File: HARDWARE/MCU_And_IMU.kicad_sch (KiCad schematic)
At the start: 16 parts, among them U2 STM32G431KBTx, Y1 Crystal_GND24

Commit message: Update footprints and add all PNs
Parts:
- BOOT_SW1: footprint (none) -> Button_Switch_THT_Custom:SW_SLW-883935-2A-D
- C11, C12, C13, C14, C15, C16: Part Number (none) -> 311-1341-2-ND
- CL1, CL2: Part Number (none) -> 311-3908-2-ND
- NRST1: footprint (none) -> Button_Switch_SMD_Custom:SW_Tactile_SPST_PTS636SK25FSMTRLFS; Part Number 108-PTS636SM43SMTRLFSTR-ND -> CKN12330-2-ND
- R4: Part Number (none) -> 311-10.0KHRTR-ND
- R5: Part Number (none) -> 311-68.0HRTR-ND
- STATUS1: footprint (none) -> LED_SMD_Custom:LED_APHBM2012QBDSURKC
- Y1: footprint (none) -> Crystal_Custom:XTAL_ECS-80-10-30B-CKM-TR
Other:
- note added: "NP0 (C0G) caps are used for the oscillator to keep frequency stable with temperature changes"
- moved on the sheet: BOOT_SW1, C11, C12, C13, C14, C15, C16, CL1, CL2, MT1, NRST1, R4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

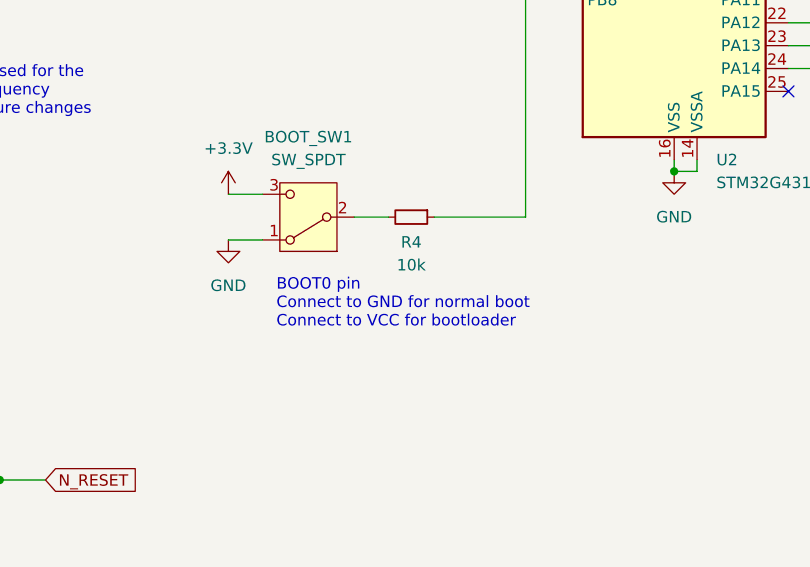
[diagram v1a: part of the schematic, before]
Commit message: Swap PWM channels and initial PCB layout
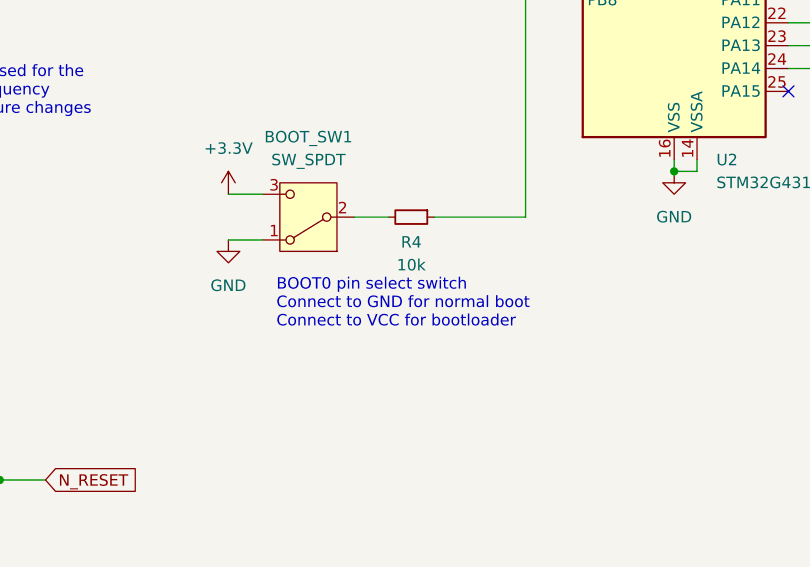
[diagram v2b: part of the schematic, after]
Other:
- note added: "BOOT0 pin select switch Connect to GND for normal boot Connect to VCC for bootloader"
- note removed: "BOOT0 pin Connect to GND for normal boot Connect to VCC for bootloader"
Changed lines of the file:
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@@
 		)
 	)
-	(text "BOOT0 pin\nConnect to GND for normal boot\nConnect to VCC for bootloader"
+	(text "BOOT0 pin select switch\nConnect to GND for normal boot\nConnect to VCC for bootloader"
 		(exclude_from_sim no)
 		(at 96.774 126.492 0)

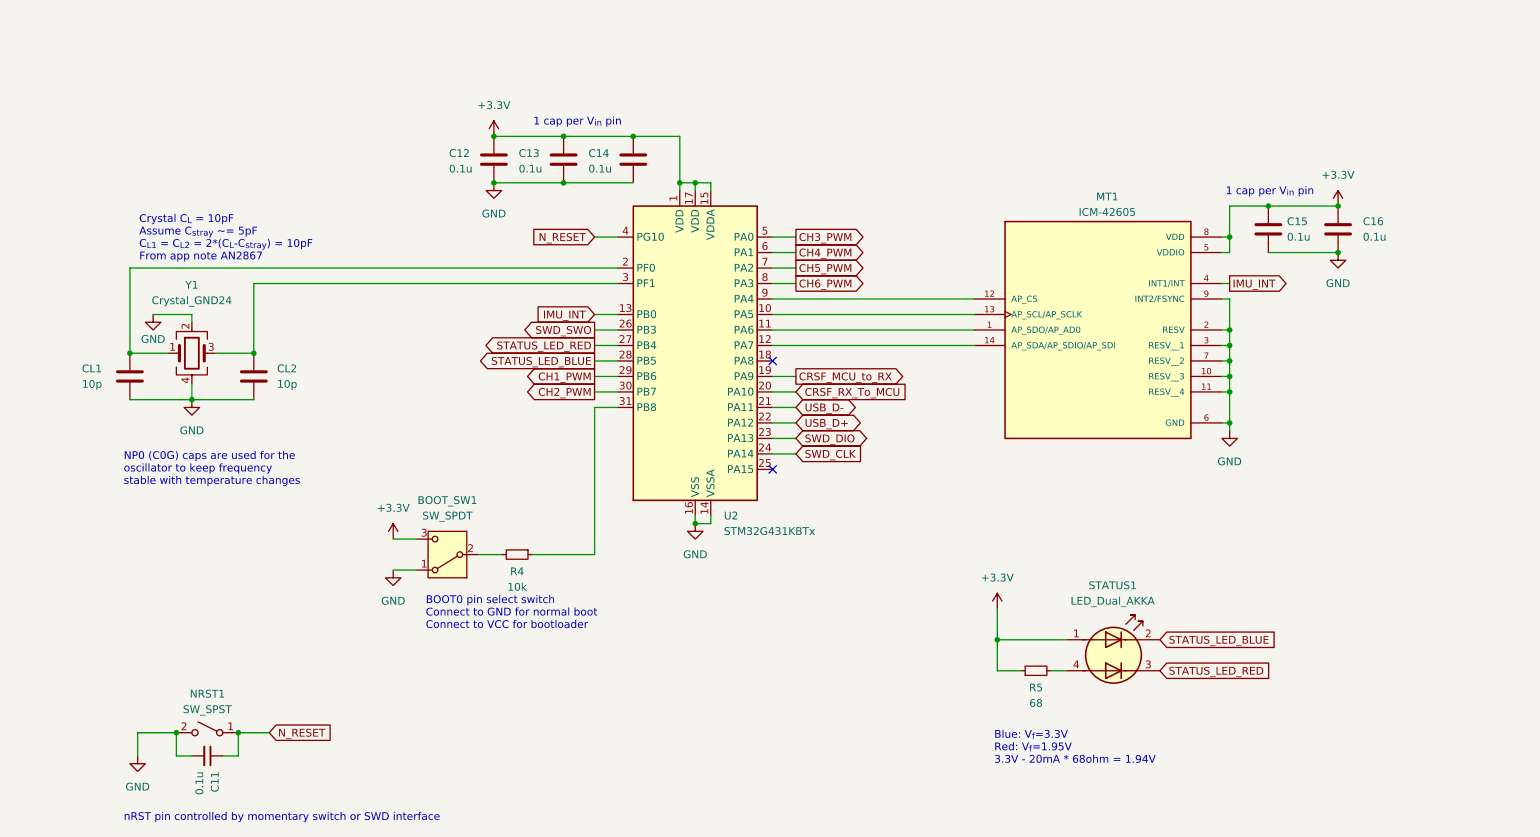
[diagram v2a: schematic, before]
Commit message: Update components and layout
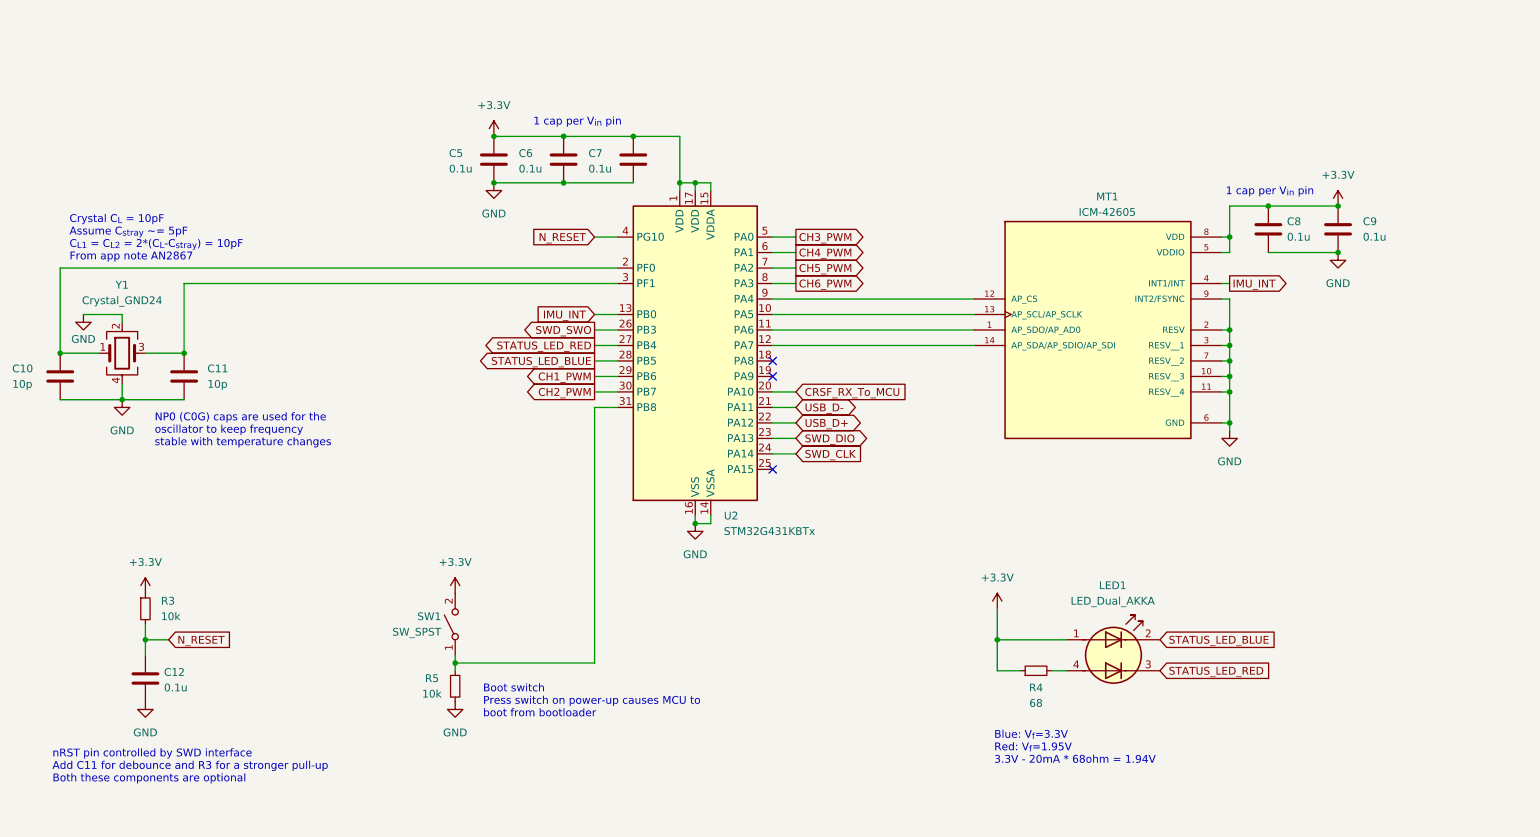
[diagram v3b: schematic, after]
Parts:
- removed BOOT_SW1: SW_SPDT, Button_Switch_THT_Custom:SW_SLW-883935-2A-D, symbol Switch:SW_SPDT
- removed C11: 0.1u, Capacitor_SMD:C_0603_1608Metric_Pad1.08x0.95mm_HandSolder, symbol Device:C_Small
- removed NRST1: SW_SPST, Button_Switch_SMD_Custom:SW_Tactile_SPST_PTS636SK25FSMTRLFS, symbol Switch:SW_SPST
- added C12: 0.1u, Capacitor_SMD:C_0402_1005Metric_Pad0.74x0.62mm_HandSolder, symbol Device:C
- added R3: 10k, Resistor_SMD:R_0402_1005Metric_Pad0.72x0.64mm_HandSolder, symbol Device:R_Small
- added SW1: SW_SPST, Button_Switch_SMD_Custom:R-667995_MIT, symbol Switch:SW_SPST
- C10: renamed from CL1; footprint Capacitor_SMD:C_0603_1608Metric_Pad1.08x0.95mm_HandSolder -> Capacitor_SMD:C_0402_1005Metric_Pad0.74x0.62mm_HandSolder; MFN (none) -> CC0402JRNPO9BN100; Part Number 311-3908-2-ND -> 311-1014-1-ND
- C11: renamed from CL2; footprint Capacitor_SMD:C_0603_1608Metric_Pad1.08x0.95mm_HandSolder -> Capacitor_SMD:C_0402_1005Metric_Pad0.74x0.62mm_HandSolder; MFN (none) -> CC0402JRNPO9BN100; Part Number 311-3908-2-ND -> 311-1014-1-ND
- C5: renamed from C12; footprint Capacitor_SMD:C_0603_1608Metric_Pad1.08x0.95mm_HandSolder -> Capacitor_SMD:C_0402_1005Metric_Pad0.74x0.62mm_HandSolder; MFN (none) -> CL05B104KA5NNNC; Part Number 311-1341-2-ND -> 1276-6720-1-ND
- C6: renamed from C13; footprint Capacitor_SMD:C_0603_1608Metric_Pad1.08x0.95mm_HandSolder -> Capacitor_SMD:C_0402_1005Metric_Pad0.74x0.62mm_HandSolder; MFN (none) -> CL05B104KA5NNNC; Part Number 311-1341-2-ND -> 1276-6720-1-ND
- C7: renamed from C14; footprint Capacitor_SMD:C_0603_1608Metric_Pad1.08x0.95mm_HandSolder -> Capacitor_SMD:C_0402_1005Metric_Pad0.74x0.62mm_HandSolder; MFN (none) -> CL05B104KA5NNNC; Part Number 311-1341-2-ND -> 1276-6720-1-ND
- C8: renamed from C15; footprint Capacitor_SMD:C_0603_1608Metric_Pad1.08x0.95mm_HandSolder -> Capacitor_SMD:C_0402_1005Metric_Pad0.74x0.62mm_HandSolder; MFN (none) -> CL05B104KA5NNNC; Part Number 311-1341-2-ND -> 1276-6720-1-ND
- C9: renamed from C16; footprint Capacitor_SMD:C_0603_1608Metric_Pad1.08x0.95mm_HandSolder -> Capacitor_SMD:C_0402_1005Metric_Pad0.74x0.62mm_HandSolder; MFN (none) -> CL05B104KA5NNNC; Part Number 311-1341-2-ND -> 1276-6720-1-ND
- LED1: renamed from STATUS1; MFN (none) -> APHBM2012QBDSURKC; Part Number 754-1506-2-ND -> 754-1506-1-ND
- MT1: MFN (none) -> ICM-42605; Part Number 1428-1152-2-ND -> 1428-1152-1-ND
- R4: renamed from R5; footprint Resistor_SMD:R_0603_1608Metric_Pad0.98x0.95mm_HandSolder -> Resistor_SMD:R_0402_1005Metric_Pad0.72x0.64mm_HandSolder; MFN (none) -> RC0402FR-0768RL; Part Number 311-68.0HRTR-ND -> 311-68.0LRCT-ND
- R5: renamed from R4; footprint Resistor_SMD:R_0603_1608Metric_Pad0.98x0.95mm_HandSolder -> Resistor_SMD:R_0402_1005Metric_Pad0.72x0.64mm_HandSolder; MFN (none) -> RC0402JR-0710KL; Part Number 311-10.0KHRTR-ND -> 311-10KJRCT-ND
- U2: MFN (none) -> STM32G431KBT6
- Y1: footprint Crystal_Custom:XTAL_ECS-80-10-30B-CKM-TR -> Crystal_Custom:Crystal_SMD_ECS_ECX_2236-4Pin_2.5x2.0mm; MFN (none) -> ECS-160-10-36-CKM-TR3; Part Number 50-ECS-80-10-30B-CKM-TR-ND -> 50-ECS-160-10-36-CKM-TR3TR-ND
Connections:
- net +3.3V: now also R3.1, SW1.2 (B)
- net GND: now also R5.2, C12.2
- net N_RESET: now also C12.1, R3.2
- net at R5.1, U2.31 (PB8): now also SW1.1 (A)
- net CRSF_MCU_to_RX: no longer names the net of U2.19 (PA9)
- no-connect marks 2 -> 3
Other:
- note added: "Boot switch Press switch on power-up causes MCU to boot from bootloader"
- note added: "nRST pin controlled by SWD interface Add C11 for debounce and R3 for a stronger pull-up Both these components are optional"
- note removed: "BOOT0 pin select switch Connect to GND for normal boot Connect to VCC for bootloader"
- note removed: "nRST pin controlled by momentary switch or SWD interface"
- moved on the sheet: C10, C11, R5, Y1

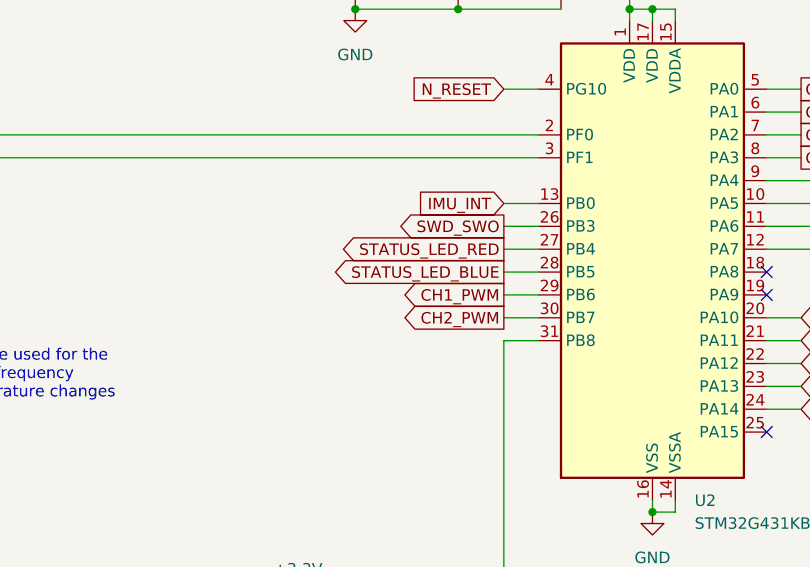
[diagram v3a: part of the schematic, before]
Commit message: Complete initial routing
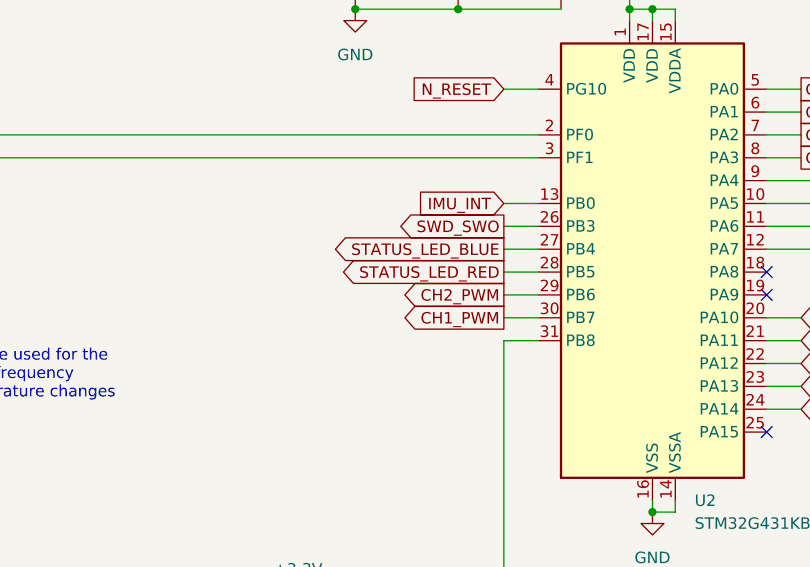
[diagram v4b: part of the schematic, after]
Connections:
- net CH1_PWM: now also U2.30 (PB7); no longer U2.29 (PB6)
- net CH2_PWM: now also U2.29 (PB6); no longer U2.30 (PB7)
- net STATUS_LED_BLUE: now also U2.27 (PB4); no longer U2.28 (PB5)
- net STATUS_LED_RED: now also U2.28 (PB5); no longer U2.27 (PB4)
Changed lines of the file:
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@@
 	(global_label "CH2_PWM"
 		(shape output)
+		(at 124.46 87.63 180)
+		(fields_autoplaced yes)
+		(effects
+			(font
+				(size 1.27 1.27)
+			)
+			(justify right)
+		)
+		(property "Intersheetrefs" "${INTERSHEET_REFS}"
+			(at 112.5244 87.63 0)
+			(effects
+				(font
+					(size 1.27 1.27)
+				)
+				(justify right)
+				(hide yes)
+			)
+		)
+	)
+	(global_label "STATUS_LED_RED"
+		(shape input)
+		(at 217.17 135.89 0)
+		(fields_autoplaced yes)
+		(effects
+			(font
+				(size 1.27 1.27)
+			)
+			(justify left)
+		)
+		(property "Intersheetrefs" "${INTERSHEET_REFS}"
+			(at 235.9998 135.89 0)
+			(effects
+				(font
+					(size 1.27 1.27)
+				)
+				(justify left)
+				(hide yes)
+			)
+		)
+	)
+	(global_label "IMU_INT"
+		(shape output)
+		(at 228.6 72.39 0)
+		(fields_autoplaced yes)
+		(effects
+			(font
+				(size 1.27 1.27)
+			)
+			(justify left)
+		)
+		(property "Intersheetrefs" "${INTERSHEET_REFS}"
+			(at 238.8424 72.39 0)
+			(effects
+				(font
+					(size 1.27 1.27)
+				)
+				(justify left)
+				(hide yes)
+			)
+		)
+	)
+	(global_label "CH5_PWM"
+		(shape output)
+		(at 157.48 69.85 0)
+		(fields_autoplaced yes)
+		(effects
+			(font
+				(size 1.27 1.27)
+			)
+			(justify left)
+		)
+		(property "Intersheetrefs" "${INTERSHEET_REFS}"
+			(at 169.4156 69.85 0)
+			(effects
+				(font
+					(size 1.27 1.27)
+				)
+				(justify left)
+				(hide yes)
+			)
+		)
+	)
+	(global_label "IMU_INT"
+		(shape input)
+		(at 124.46 77.47 180)
+		(fields_autoplaced yes)
+		(effects
+			(font
+				(size 1.27 1.27)
+			)
+			(justify right)
+		)
+		(property "Intersheetrefs" "${INTERSHEET_REFS}"
+			(at 114.2176 77.47 0)
+			(effects
+				(font
+					(size 1.27 1.27)
+				)
+				(justify right)
+				(hide yes)
+			)
+		)
+	)
+	(global_label "CRSF_RX_To_MCU"
+		(shape input)
+		(at 157.48 90.17 0)
+		(fields_autoplaced yes)
+		(effects
+			(font
+				(size 1.27 1.27)
+			)
+			(justify left)
+		)
+		(property "Intersheetrefs" "${INTERSHEET_REFS}"
+			(at 176.8541 90.17 0)
+			(effects
+				(font
+					(size 1.27 1.27)
+				)
+				(justify left)
+				(hide yes)
+			)
+		)
+	)
+	(global_label "CH6_PWM"
+		(shape output)
+		(at 157.48 72.39 0)
+		(fields_autoplaced yes)
+		(effects
+			(font
+				(size 1.27 1.27)
+			)
+			(justify left)
+		)
+		(property "Intersheetrefs" "${INTERSHEET_REFS}"
+			(at 169.4156 72.39 0)
+			(effects
+				(font
+					(size 1.27 1.27)
+				)
+				(justify left)
+				(hide yes)
+			)
+		)
+	)
+	(global_label "CH1_PWM"
+		(shape output)
 		(at 124.46 90.17 180)
 		(fields_autoplaced yes)
@@
 		)
 	)
+	(global_label "SWD_SWO"
+		(shape output)
+		(at 124.46 80.01 180)
+		(fields_autoplaced yes)
+		(effects
+			(font
+				(size 1.27 1.27)
+			)
+			(justify right)
+		)
+		(property "Intersheetrefs" "${INTERSHEET_REFS}"
+			(at 112.5849 80.01 0)
+			(effects
+				(font
+					(size 1.27 1.27)
+				)
+				(justify right)
+				(hide yes)
+			)
+		)
+	)
+	(global_label "STATUS_LED_BLUE"
+		(shape input)
+		(at 217.17 130.81 0)
+		(fields_autoplaced yes)
+		(effects
+			(font
+				(size 1.27 1.27)
+			)
+			(justify left)
+		)
+		(property "Intersheetrefs" "${INTERSHEET_REFS}"
+			(at 237.0884 130.81 0)
+			(effects
+				(font
+					(size 1.27 1.27)
+				)
+				(justify left)
+				(hide yes)
+			)
+		)
+	)
 	(global_label "STATUS_LED_RED"
-		(shape input)
-		(at 217.17 135.89 0)
-		(fields_autoplaced yes)
-		(effects
-			(font
-				(size 1.27 1.27)
-			)
-			(justify left)
-		)
-		(property "Intersheetrefs" "${INTERSHEET_REFS}"
-			(at 235.9998 135.89 0)
-			(effects
-				(font
-					(size 1.27 1.27)
-				)
-				(justify left)
-				(hide yes)
-			)
-		)
-	)
-	(global_label "IMU_INT"
-		(shape output)
-		(at 228.6 72.39 0)
-		(fields_autoplaced yes)
-		(effects
-			(font
-				(size 1.27 1.27)
-			)
-			(justify left)
-		)
-		(property "Intersheetrefs" "${INTERSHEET_REFS}"
-			(at 238.8424 72.39 0)
-			(effects
-				(font
-					(size 1.27 1.27)
-				)
-				(justify left)
-				(hide yes)
-			)
-		)
-	)
-	(global_label "CH5_PWM"
-		(shape output)
-		(at 157.48 69.85 0)
-		(fields_autoplaced yes)
-		(effects
-			(font
-				(size 1.27 1.27)
-			)
-			(justify left)
-		)
-		(property "Intersheetrefs" "${INTERSHEET_REFS}"
-			(at 169.4156 69.85 0)
-			(effects
-				(font
-					(size 1.27 1.27)
-				)
-				(justify left)
-				(hide yes)
-			)
-		)
-	)
-	(global_label "IMU_INT"
-		(shape input)
-		(at 124.46 77.47 180)
-		(fields_autoplaced yes)
-		(effects
-			(font
-				(size 1.27 1.27)
-			)
-			(justify right)
-		)
-		(property "Intersheetrefs" "${INTERSHEET_REFS}"
-			(at 114.2176 77.47 0)
-			(effects
-				(font
-					(size 1.27 1.27)
-				)
-				(justify right)
-				(hide yes)
-			)
-		)
-	)
-	(global_label "CRSF_RX_To_MCU"
-		(shape input)
-		(at 157.48 90.17 0)
-		(fields_autoplaced yes)
-		(effects
-			(font
-				(size 1.27 1.27)
-			)
-			(justify left)
-		)
-		(property "Intersheetrefs" "${INTERSHEET_REFS}"
-			(at 176.8541 90.17 0)
-			(effects
-				(font
-					(size 1.27 1.27)
-				)
-				(justify left)
-				(hide yes)
-			)
-		)
-	)
-	(global_label "CH6_PWM"
-		(shape output)
-		(at 157.48 72.39 0)
-		(fields_autoplaced yes)
-		(effects
-			(font
-				(size 1.27 1.27)
-			)
-			(justify left)
-		)
-		(property "Intersheetrefs" "${INTERSHEET_REFS}"
-			(at 169.4156 72.39 0)
-			(effects
-				(font
-					(size 1.27 1.27)
-				)
-				(justify left)
-				(hide yes)
-			)
-		)
-	)
-	(global_label "CH1_PWM"
-		(shape output)
-		(at 124.46 87.63 180)
-		(fields_autoplaced yes)
-		(effects
-			(font
-				(size 1.27 1.27)
-			)
-			(justify right)
-		)
-		(property "Intersheetrefs" "${INTERSHEET_REFS}"
-			(at 112.5244 87.63 0)
-			(effects
-				(font
-					(size 1.27 1.27)
-				)
-				(justify right)
-				(hide yes)
-			)
-		)
-	)
-	(global_label "SWD_SWO"
-		(shape output)
-		(at 124.46 80.01 180)
-		(fields_autoplaced yes)
-		(effects
-			(font
-				(size 1.27 1.27)
-			)
-			(justify right)
-		)
-		(property "Intersheetrefs" "${INTERSHEET_REFS}"
-			(at 112.5849 80.01 0)
-			(effects
-				(font
-					(size 1.27 1.27)
-				)
-				(justify right)
-				(hide yes)
-			)
-		)
-	)
-	(global_label "STATUS_LED_BLUE"
-		(shape input)
-		(at 217.17 130.81 0)
-		(fields_autoplaced yes)
-		(effects
-			(font
-				(size 1.27 1.27)
-			)
-			(justify left)
-		)
-		(property "Intersheetrefs" "${INTERSHEET_REFS}"
-			(at 237.0884 130.81 0)
-			(effects
-				(font
-					(size 1.27 1.27)
-				)
-				(justify left)
-				(hide yes)
-			)
-		)
-	)
-	(global_label "STATUS_LED_RED"
-		(shape output)
-		(at 124.46 82.55 180)
-		(fields_autoplaced yes)
-		(effects
-			(font
-				(size 1.27 1.27)
-			)
-			(justify right)
-		)
-		(property "Intersheetrefs" "${INTERSHEET_REFS}"
-			(at 105.6302 82.55 0)
+		(shape output)
+		(at 124.46 85.09 180)
+		(fields_autoplaced yes)
+		(effects
+			(font
+				(size 1.27 1.27)
+			)
+			(justify right)
+		)
+		(property "Intersheetrefs" "${INTERSHEET_REFS}"
+			(at 105.6302 85.09 0)
 			(effects
 				(font
@@
 	(global_label "STATUS_LED_BLUE"
 		(shape output)
-		(at 124.46 85.09 180)
-		(fields_autoplaced yes)
-		(effects
-			(font
-				(size 1.27 1.27)
-			)
-			(justify right)
-		)
-		(property "Intersheetrefs" "${INTERSHEET_REFS}"
-			(at 104.5416 85.09 0)
-			(effects
-				(font
+		(at 124.46 82.55 180)
+		(fields_autoplaced yes)
+		(effects
+			(font
+				(size 1.27 1.27)
+			)
+			(justify right)
+		)
+		(property "Intersheetrefs" "${INTERSHEET_REFS}"
+			(at 104.5416 82.55 0)
+			(effects
+				(font
